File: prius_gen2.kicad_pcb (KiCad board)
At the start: 4 copper layers, 147.8 x 65 mm, 149 parts, among them J1 Conn_02x05_Odd_Even, J2 Conn_01x06, J3 Conn_01x23, J4 Conn_01x14, J5 Conn_01x03_Male, Q1 IRLZ14SPBF, Q2 IRLZ14SPBF, SW1 SW_Push, SW2 SW_Push, SW3 RESET, SW4 BOOT, U2 MCP602, U3 ULN2003A, U4 TDA2822D, U5 TJA1051T-3, U6 ESP32-WROOM-32, U7 LMR14020, U8 AZ1117-3.3, U9 STM32F103VBTx, Y1 8MHz

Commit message: started adding AD2S
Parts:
- removed C20: 1uF, Capacitor_SMD:C_0603_1608Metric
- removed C21: 100uF, Capacitor_SMD:C_Elec_6.3x7.7
- removed C22, C23, C24, C25, C27: 22n, Capacitor_SMD:C_0603_1608Metric
- removed C26: 10u, Capacitor_SMD:C_0603_1608Metric
- removed the C28 at (117.7, 113.3)
- removed the C29 at (117.7, 100.1)
- removed the C30 at (208.2, 124.3)
- removed the C31 at (180.4, 115.9)
- removed the C32 at (182.4, 115.9)
- removed the C33 at (157.3, 102.1)
- removed C45, C46, C47, C48, C49, C51, C52: 1u, Capacitor_SMD:C_0603_1608Metric
- removed the D3 at (177.2, 95.5)
- removed J5: Conn_01x03_Male, Connector_PinSocket_1.27mm:PinSocket_1x03_P1.27mm_Vertical_SMD_Pin1Left
- removed Q1, Q2: IRLZ14SPBF, Package_TO_SOT_SMD:TO-252-2
- removed the R27 at (94.6, 103.8)
- removed the R28 at (98.2, 103.8)
- removed the R29 at (101.8, 103.8)
- removed the R30 at (106.2, 107.4)
- removed the R31 at (117.7, 110.0)
- removed the R32 at (117.7, 103.4)
- removed the R34 at (208.2, 120.1)
- removed the R35 at (174.2, 95.5)
- removed the R36 at (157.4, 100.1)
- removed the R45 at (99.2, 99.5)
- removed R46, R47, R48, R49: 3.3k, Resistor_SMD:R_0603_1608Metric
- removed R50, R51, R52, R53, R54: 1.2k, Resistor_SMD:R_0603_1608Metric
- removed R56, R57, R60, R61, R62, R63: 10k, Resistor_SMD:R_0603_1608Metric
- removed SW3: RESET, Button_Switch_SMD:SW_SPST_EVQQ2
- removed SW4: BOOT, Button_Switch_SMD:SW_SPST_EVQQ2
- removed the U4 at (112.6, 106.0)
- removed the U6 at (169.0, 108.4)
- removed U9: STM32F103VBTx, Package_QFP:LQFP-100_14x14mm_P0.5mm
- added C18: 20pF, Capacitor_SMD:C_0603_1608Metric, F.Cu at (108.0, 88.2)
- added C19: 20pF, Capacitor_SMD:C_0603_1608Metric, F.Cu at (104.8, 88.2)
- added TP1: TestPoint, TestPoint:TestPoint_Keystone_5000-5004_Miniature, F.Cu at (144.5, 75.7)
- added TP2: TestPoint, TestPoint:TestPoint_Keystone_5000-5004_Miniature, F.Cu at (154.4, 86.6)
- added TP3: TestPoint, TestPoint:TestPoint_Keystone_5000-5004_Miniature, F.Cu at (166.9, 111.2)
- added TP4: TestPoint, TestPoint:TestPoint_Keystone_5000-5004_Miniature, F.Cu at (172.0, 111.2)
- added TP5: TestPoint, TestPoint:TestPoint_Keystone_5000-5004_Miniature, F.Cu at (161.9, 111.2)
- added TP6: TestPoint, TestPoint:TestPoint_Keystone_5000-5004_Miniature, F.Cu at (166.9, 106.2)
- added TP7: TestPoint, TestPoint:TestPoint_Keystone_5000-5004_Miniature, F.Cu at (161.9, 106.2)
- added U1: STM32F407VETx, Package_QFP:LQFP-100_14x14mm_P0.5mm, F.Cu at (138.2, 93.2)
- added U3: AD2S1205YSTZ, ad2s:QFP80P1200X1200X160-44N, F.Cu at (111.4, 101.2)
- added Y2: 8.192MHz, Crystal:Crystal_SMD_5032-2Pin_5.0x3.2mm, F.Cu at (106.4, 91.2)
- renumbered C7 to C10, C8 to C11, C9 to C12, C43 to C13, C44 to C14, C50 to C15, C18 to C16, C19 to C17, C13 to C28, C34 to C29, C10 to C3, C35 to C30, C36 to C31, C37 to C32, C38 to C33, C39 to C34, C40 to C35, C41 to C36, C42 to C37, C14 to C38, C15 to C39, C16 to C40, C17 to C41, C11 to C5, C12 to C6, C3 to C7, C5 to C8, C6 to C9, D7 to D1, D1 to D2, D2 to D3, JP2 to JP1, JP3 to JP2, JP1 to JP3, R44 to R10, R55 to R11, R58 to R12, R59 to R13, R22 to R14, R23 to R15, R24 to R16, R25 to R17, R26 to R18, R3 to R2, R33 to R25, R37 to R26, R38 to R27, R39 to R28, R40 to R29, R5 to R3, R6 to R30, R7 to R31, R8 to R32, R9 to R33, R10 to R34, R11 to R35, R12 to R36, R13 to R37, R14 to R38, R15 to R39, R16 to R40, R17 to R41, R18 to R42, R19 to R43, R20 to R44, R21 to R45, R64 to R5, R2 to R6, R41 to R7, R42 to R8, R43 to R9, U3 to U2, U5 to U4, U7 to U5, U8 to U6, U2 to U7
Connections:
- net Net-(J4-Pad10) renamed /Connectors/MVU
- net Net-(J4-Pad11) renamed /Connectors/MUU
- net Net-(J4-Pad9) renamed /Connectors/MWU
- J1 pad 6: Net-(J1-Pad6) -> unconnected-(J1-Pad6)
- J1 pad 7: Net-(J1-Pad7) -> unconnected-(J1-Pad7)
- J1 pad 8: Net-(J1-Pad8) -> unconnected-(J1-Pad8)
- J2 pad 6: Net-(J2-Pad6) -> unconnected-(J2-Pad6)
- J3 pad 10: /SIG_BRAKE -> unconnected-(J3-Pad10)
- J3 pad 11: /SIG_FWD -> unconnected-(J3-Pad11)
- J3 pad 12: /SIG_REV -> unconnected-(J3-Pad12)
- J3 pad 15: /OUT_DCSW -> unconnected-(J3-Pad15)
- J3 pad 16: /OUT_PRE -> unconnected-(J3-Pad16)
- J3 pad 7: /THROTTLE1 -> unconnected-(J3-Pad7)
- J3 pad 8: /THROTTLE2 -> unconnected-(J3-Pad8)
- J3 pad 9: /SIG_START -> unconnected-(J3-Pad9)
- J4 pad 8: Net-(J4-Pad8) -> unconnected-(J4-Pad8)
- U2 pad 13: Net-(J4-Pad8) -> unconnected-(U2-Pad13)
- U2 pad 14: Net-(U3-Pad14) -> unconnected-(U2-Pad14)
- U2 pad 3: Net-(U3-Pad3) -> unconnected-(U2-Pad3)
- U2 pad 4: /TIM1_CH2N -> unconnected-(U2-Pad4)
- U2 pad 9: Net-(U3-Pad9) -> unconnected-(U2-Pad9)
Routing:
- net /ADC9: track 84.0 -> 0.00 mm, vias 2 -> 0
- net /ADC11: track 81.5 -> 0.00 mm, vias 2 -> 0
- net /ADC10: track 78.4 -> 0.00 mm, vias 2 -> 0
- net /PC13: track 68.9 -> 0.00 mm, vias 2 -> 0
- net Net-(J4-Pad8): track 65.3 -> 0.00 mm
- net +3V3: track 280.0 -> 214.7 mm, vias 18 -> 15
- net unconnected-(J4-Pad8): track 0.00 -> 62.1 mm
- net Net-(C33-Pad1) (its old number): track 54.9 -> 0.00 mm, vias 2 -> 0
- net /ADC2: track 52.0 -> 0.00 mm, vias 2 -> 0
- net /ADC3: track 48.7 -> 0.00 mm, vias 2 -> 0
- net /ADC4: track 48.2 -> 0.00 mm, vias 2 -> 0
- net GND: track 121.7 -> 75.4 mm, vias 124 -> 75
- net /REV: track 44.9 -> 0.00 mm, vias 2 -> 0
- net /TIM4_CH1: track 43.8 -> 0.00 mm, vias 2 -> 0
- net /TIM3_ETR: track 42.1 -> 0.00 mm
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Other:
- board text added: "Prius G2 rev 4 2022-12"
- board text added: "github.com/ksmola/PriusG2"
- board text removed: "DCSW"
- board text removed: "ESP"
- board text removed: "FIL"
- board text removed: "PRE"
- board text removed: "Prius G2 rev 3 2021-08"
- board text removed: "TH2"
- board text removed: "powered by openinverter.org github.com/ksmola/PriusG2"

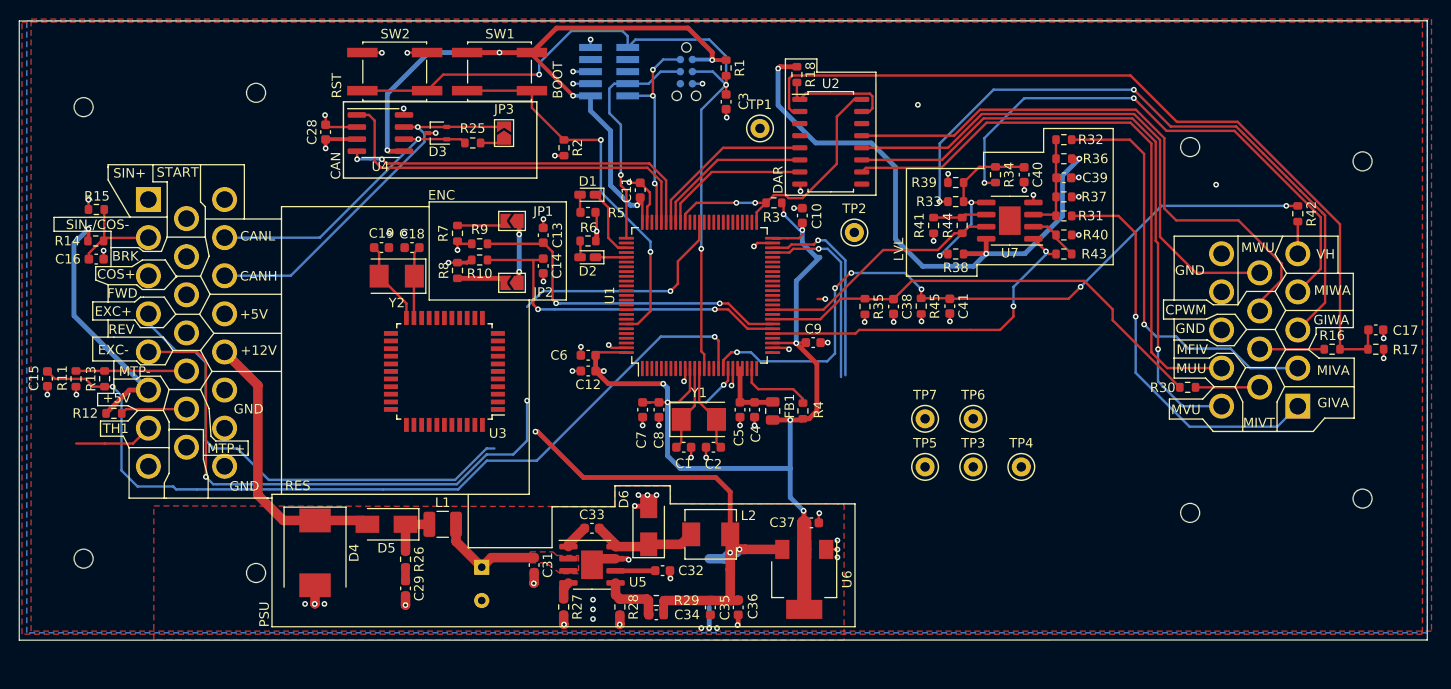
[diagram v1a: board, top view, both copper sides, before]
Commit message: routed ad2s
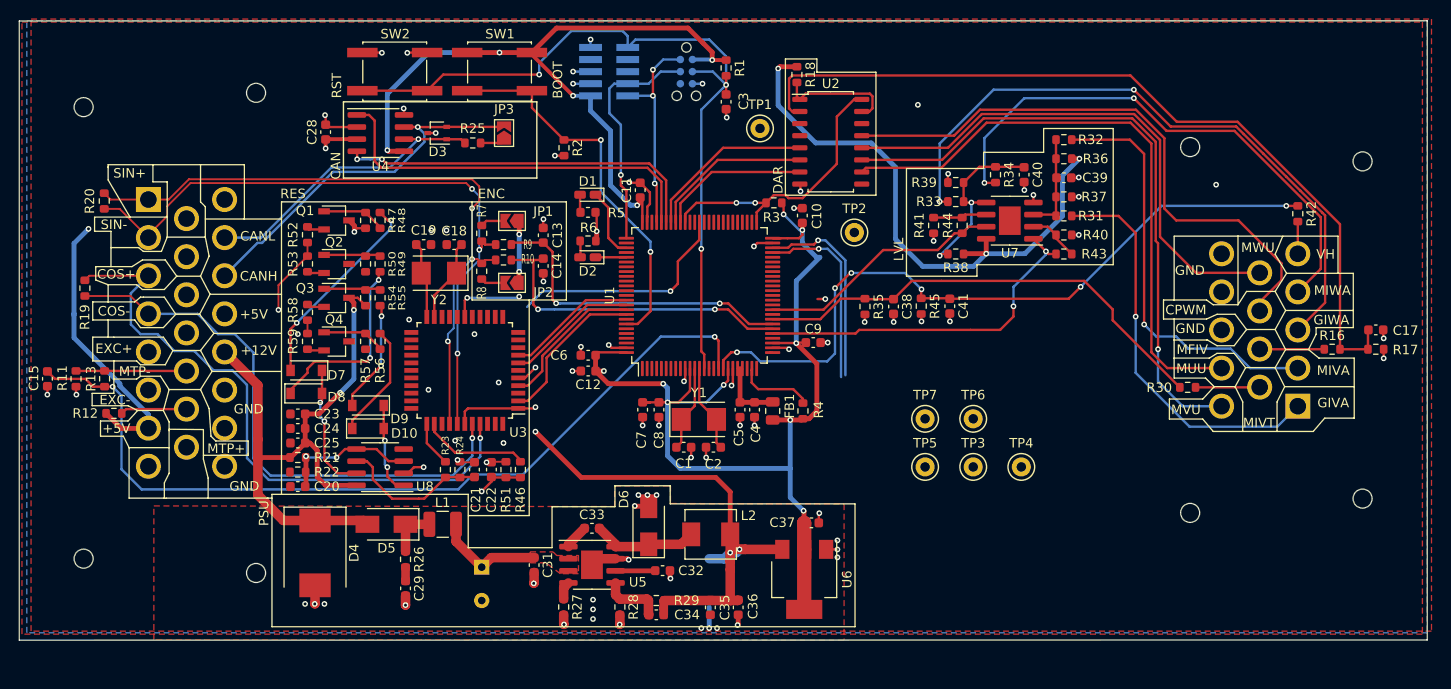
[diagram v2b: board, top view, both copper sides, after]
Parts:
- removed C16: 10uF, Capacitor_SMD:C_0603_1608Metric
- removed R14: 510, Resistor_SMD:R_0603_1608Metric
- removed R15: 220, Resistor_SMD:R_0603_1608Metric
- added C20: .1uF, Capacitor_SMD:C_0603_1608Metric, F.Cu at (96.0, 113.3)
- added C21: 120pF, Capacitor_SMD:C_0603_1608Metric, F.Cu at (114.6, 111.5)
- added C22: 120pF, Capacitor_SMD:C_0603_1608Metric, F.Cu at (116.3, 111.5)
- added C23: 1uF 12mR, Capacitor_SMD:C_0603_1608Metric, F.Cu at (96.0, 105.7)
- added C24: 1uF 12mR, Capacitor_SMD:C_0603_1608Metric, F.Cu at (96.0, 107.2)
- added C25: 10nF, Capacitor_SMD:C_0603_1608Metric, F.Cu at (96.0, 108.7)
- added D10: D, Diode_SMD:D_SOD-123, F.Cu at (103.4, 107.2)
- added D7: D, Diode_SMD:D_SOD-123, F.Cu at (96.9, 101.1)
- added D8: D, Diode_SMD:D_SOD-123, F.Cu at (96.9, 103.5)
- added D9: D, Diode_SMD:D_SOD-123, F.Cu at (103.4, 104.8)
- added Q1: Q_NPN_BEC, Package_TO_SOT_SMD:TSOT-23, F.Cu at (100.1, 85.3)
- added Q2: Q_PNP_BEC, Package_TO_SOT_SMD:TSOT-23, F.Cu at (100.1, 89.9)
- added Q3: Q_NPN_BEC, Package_TO_SOT_SMD:TSOT-23, F.Cu at (100.1, 93.5)
- added Q4: Q_PNP_BEC, Package_TO_SOT_SMD:TSOT-23, F.Cu at (100.1, 98.0)
- added R19: 68k, Resistor_SMD:R_0603_1608Metric, F.Cu at (73.7, 92.5)
- added R20: 68k, Resistor_SMD:R_0603_1608Metric, F.Cu at (75.7, 83.3)
- added R21: 22k, Resistor_SMD:R_0603_1608Metric, F.Cu at (96.0, 110.2)
- added R22: 10k, Resistor_SMD:R_0603_1608Metric, F.Cu at (96.0, 111.8)
- added R23: 10k, Resistor_SMD:R_0603_1608Metric, F.Cu at (111.5, 111.5)
- added R24: R, Resistor_SMD:R_0603_1608Metric, F.Cu at (113.0, 111.5)
- added R46: 10k, Resistor_SMD:R_0603_1608Metric, F.Cu at (119.4, 111.5)
- added R47: 2k2, Resistor_SMD:R_0603_1608Metric, F.Cu at (103.1, 85.3)
- added R48: 3r3, Resistor_SMD:R_0603_1608Metric, F.Cu at (104.6, 85.3)
- added R49: 3r3, Resistor_SMD:R_0603_1608Metric, F.Cu at (104.6, 89.9)
- added R50: 2k2, Resistor_SMD:R_0603_1608Metric, F.Cu at (103.1, 89.9)
- added R51: R, Resistor_SMD:R_0603_1608Metric, F.Cu at (117.9, 111.5)
- added R52: 4r7, Resistor_SMD:R_0603_1608Metric, F.Cu at (97.0, 86.8)
- added R53: 4r7, Resistor_SMD:R_0603_1608Metric, F.Cu at (97.0, 89.9)
- added R54: 2k2, Resistor_SMD:R_0603_1608Metric, F.Cu at (103.1, 93.5)
- added R55: 3r3, Resistor_SMD:R_0603_1608Metric, F.Cu at (104.6, 93.5)
- added R56: 3r3, Resistor_SMD:R_0603_1608Metric, F.Cu at (104.6, 98.0)
- added R57: 2k2, Resistor_SMD:R_0603_1608Metric, F.Cu at (103.1, 98.0)
- added R58: 4r7, Resistor_SMD:R_0603_1608Metric, F.Cu at (97.0, 95.0)
- added R59: 4r7, Resistor_SMD:R_0603_1608Metric, F.Cu at (97.0, 98.0)
- added U8: AD8676xR, Package_SO:SOIC-8_3.9x4.9mm_P1.27mm, F.Cu at (104.6, 111.3)
- C18, C19: value 20pF -> 22pF
- moved C18 4.43 mm to (112.4, 87.9)
- moved C19 4.43 mm to (109.2, 87.9)
- moved Y2 4.43 mm to (110.8, 90.9)
- moved R8 2.54 mm to (115.3, 90.7)
- moved R7 2.54 mm to (115.3, 86.7)
- moved R9 2.50 mm to (117.6, 87.9)
- moved R10 2.50 mm to (117.6, 89.5)
- moved U3 2.14 mm to (113.5, 101.1)
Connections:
- C13 pad 1: /TIM3_CH2 -> /Input Filter/TIM3_CH2
- C14 pad 1: /TIM3_CH1 -> /Input Filter/TIM3_CH1
- C38 pad 1: /ADC14 -> /Level Shifting/ADC14
- C41 pad 1: /ADC13 -> /Level Shifting/ADC13
- J3 pad 1: /ENC_B -> /SIN+
- J3 pad 2: Net-(C16-Pad1) -> /SIN-
- J3 pad 3: /ENC_A -> /COS+
- J3 pad 4: /R1 -> /COS-
- J3 pad 5: /R2 -> /EXC+
- J3 pad 6: +5V -> /EXC-
- J3 pad 7: unconnected-(J3-Pad7) -> +5V
- R10 pad 1: /TIM3_CH1 -> /Input Filter/TIM3_CH1
- R10 pad 2: /ENC_A -> /SIN+
- R11 pad 1: /MTEMP- -> /Input Filter/MTEMP-
- R12 pad 1: /MTEMP+ -> /Input Filter/MTEMP+
- R13 pad 1: /MTEMP- -> /Input Filter/MTEMP-
- R30 pad 1: /ADC14 -> /Level Shifting/ADC14
- R30 pad 2: /MIVT -> /Level Shifting/MIVT
- R31 pad 2: /Connectors/GIVA -> /Level Shifting/GIVA
- R32 pad 2: /Connectors/MIVA -> /Level Shifting/MIVA
- R33 pad 2: /Connectors/GIWA -> /Level Shifting/GIWA
- R34 pad 2: /Connectors/MIWA -> /Level Shifting/MIWA
- R35 pad 1: /ADC14 -> /Level Shifting/ADC14
- R42 pad 1: /ADC13 -> /Level Shifting/ADC13
- R42 pad 2: /VH -> /Level Shifting/VH
- R43 pad 2: /ADC5 -> /Level Shifting/ADC5
- R44 pad 2: /ADC8 -> /Level Shifting/ADC8
- R45 pad 1: /ADC13 -> /Level Shifting/ADC13
- R7 pad 2: /ENC_B -> /SIN-
- R8 pad 2: /ENC_A -> /SIN+
- R9 pad 1: /TIM3_CH2 -> /Input Filter/TIM3_CH2
- R9 pad 2: /ENC_B -> /SIN-
- U1 pad 89: unconnected-(U1-Pad89) -> /SCLK
- U1 pad 90: unconnected-(U1-Pad90) -> /MISO
- U1 pad 91: unconnected-(U1-Pad91) -> /~{SAMPLE}
- U1 pad 92: unconnected-(U1-Pad92) -> /~{CS}
- U3 pad 34: unconnected-(U3-Pad34) -> /Resolver/T_EXC
- U3 pad 35: unconnected-(U3-Pad35) -> /Resolver/~{T_EXC}
- U3 pad 36: unconnected-(U3-Pad36) -> GND
- U3 pad 37: /Resolver/SIN -> /SIN+
- U3 pad 38: /Resolver/~{SIN} -> /SIN-
- U3 pad 39: unconnected-(U3-Pad39) -> +5V
- U3 pad 40: /Resolver/~{COS} -> /COS-
- U3 pad 41: /Resolver/COS -> /COS+
- U3 pad 42: unconnected-(U3-Pad42) -> GND
- U4 pad 1: /CAN_TX -> /Communication/TXDCAN
- U4 pad 4: /CAN_RX -> /Communication/RXDCAN
- U7 pad 1: /ADC5 -> /Level Shifting/ADC5
- U7 pad 7: /ADC8 -> /Level Shifting/ADC8
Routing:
- net /Level Shifting/ADC13: track 0.00 -> 75.5 mm, vias 0 -> 6
- net /ADC13: track 75.5 -> 0.00 mm, vias 6 -> 0
- net /SIN-: track 0.00 -> 72.4 mm, vias 0 -> 3
- net /SIN+: track 0.00 -> 70.4 mm, vias 0 -> 3
- net /Level Shifting/GIWA: track 0.00 -> 68.4 mm, vias 0 -> 2
- net /Connectors/GIWA: track 68.4 -> 0.00 mm, vias 2 -> 0
- net /COS+: track 0.00 -> 65.1 mm, vias 0 -> 1
- net /COS-: track 0.00 -> 60.2 mm, vias 0 -> 1
- net /R2: track 58.7 -> 0.00 mm, vias 2 -> 0
- net /EXC+: track 0.00 -> 51.2 mm, vias 0 -> 2
- net /R1: track 50.3 -> 0.00 mm
- net /Level Shifting/ADC14: track 0.00 -> 49.8 mm
- net /ADC14: track 49.8 -> 0.00 mm
- net /EXC-: track 0.00 -> 49.3 mm, vias 0 -> 2
- net +12V: track 29.7 -> 76.6 mm, vias 0 -> 3
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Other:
- board text added: "COS-"
- board text added: "SIN-"
- board text removed: "BRK"
- board text removed: "FWD"
- board text removed: "REV"
- board text removed: "SIN-/COS-"
- board text removed: "START"
- board text removed: "TH1"

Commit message: cleaned up board
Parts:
- TP1, TP2, TP3, TP4, TP5, TP6, TP7: moved to B.Cu
- moved R32 45.1 mm to (183.4, 121.4), turned to -90 degrees
- moved R36 42.8 mm to (181.4, 121.4), turned to 90 degrees
- moved C39 40.7 mm to (179.4, 121.4), turned to -90 degrees
- moved R37 38.6 mm to (177.4, 121.4), turned to -90 degrees
- moved C40 37.5 mm to (179.7, 117.2), turned to 180 degrees
- moved R31 36.6 mm to (175.4, 121.4), turned to -90 degrees
- moved R34 35.3 mm to (179.7, 114.2), turned to 180 degrees
- moved R40 34.7 mm to (173.4, 121.4), turned to -90 degrees
- moved R43 32.9 mm to (171.4, 121.4), turned to 90 degrees
- moved R39 31.9 mm to (178.9, 110.1), turned to 90 degrees
- moved U7 30.7 mm to (174.9, 115.7), turned to 90 degrees
- moved TP3 30.4 mm to (153.7, 83.9), turned to 180 degrees
- moved R33 29.2 mm to (176.9, 110.1), turned to 90 degrees
- moved R44 26.3 mm to (174.4, 110.7), turned to 180 degrees
- moved R41 24.8 mm to (174.4, 107.7), turned to 180 degrees
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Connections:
- C13 pad 1: /Input Filter/TIM3_CH2 -> /TIM3_CH2
- C14 pad 1: /Input Filter/TIM3_CH1 -> /TIM3_CH1
- C38 pad 1: /Level Shifting/ADC14 -> /ADC14
- C41 pad 1: /Level Shifting/ADC13 -> /ADC13
- R10 pad 1: /Input Filter/TIM3_CH1 -> /TIM3_CH1
- R11 pad 1: /Input Filter/MTEMP- -> /MTEMP-
- R12 pad 1: /Input Filter/MTEMP+ -> /MTEMP+
- R13 pad 1: /Input Filter/MTEMP- -> /MTEMP-
- R30 pad 1: /Level Shifting/ADC14 -> /ADC14
- R30 pad 2: /Level Shifting/MIVT -> /MIVT
- R31 pad 2: /Level Shifting/GIVA -> /Connectors/GIVA
- R32 pad 2: /Level Shifting/MIVA -> /Connectors/MIVA
- R33 pad 2: /Level Shifting/GIWA -> /Connectors/GIWA
- R34 pad 2: /Level Shifting/MIWA -> /Connectors/MIWA
- R35 pad 1: /Level Shifting/ADC14 -> /ADC14
- R42 pad 1: /Level Shifting/ADC13 -> /ADC13
- R42 pad 2: /Level Shifting/VH -> /VH
- R43 pad 2: /Level Shifting/ADC5 -> /ADC5
- R44 pad 2: /Level Shifting/ADC8 -> /ADC8
- R45 pad 1: /Level Shifting/ADC13 -> /ADC13
- R9 pad 1: /Input Filter/TIM3_CH2 -> /TIM3_CH2
- U3 pad 2: /Resolver/~{RD} -> /~{CS}
- U3 pad 4: /Resolver/~{SAMPLE} -> /~{SAMPLE}
- U3 pad 7: /Resolver/SO -> /MISO
- U3 pad 8: /Resolver/SCLK -> /SCLK
- U4 pad 1: /Communication/TXDCAN -> /CAN_TX
- U4 pad 4: /Communication/RXDCAN -> /CAN_RX
- U7 pad 1: /Level Shifting/ADC5 -> /ADC5
- U7 pad 7: /Level Shifting/ADC8 -> /ADC8
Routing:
- net /Level Shifting/ADC13: track 75.5 -> 0.00 mm, vias 6 -> 0
- net /Level Shifting/GIWA: track 68.4 -> 0.00 mm, vias 2 -> 0
- net +5V: track 309.4 -> 245.3 mm, vias 14 -> 11
- net unconnected-(J4-Pad8): track 62.1 -> 0.00 mm
- net /ADC13: track 0.00 -> 56.9 mm, vias 0 -> 3
- net /Level Shifting/ADC14: track 49.8 -> 0.00 mm
- net /Level Shifting/MIVA: track 44.1 -> 0.00 mm, vias 1 -> 0
- net /Level Shifting/GIVA: track 42.4 -> 0.00 mm, vias 1 -> 0
- net /Connectors/GIWA: track 0.00 -> 39.0 mm, vias 0 -> 1
- net /Communication/RXDCAN: track 38.6 -> 0.00 mm, vias 2 -> 0
- net /CAN_RX: track 0.00 -> 38.6 mm, vias 0 -> 2
- net /Level Shifting/ADC5: track 37.3 -> 0.00 mm, vias 2 -> 0
- net /TIM3_CH1: track 0.00 -> 34.3 mm, vias 0 -> 2
- net /Input Filter/TIM3_CH1: track 34.3 -> 0.00 mm, vias 2 -> 0
- net /Input Filter/TIM3_CH2: track 34.2 -> 0.00 mm, vias 2 -> 0
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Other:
- board size 147.8 x 65 mm -> 130.6 x 65 mm
- board text removed: "CPWM"
- board text removed: "LVL"

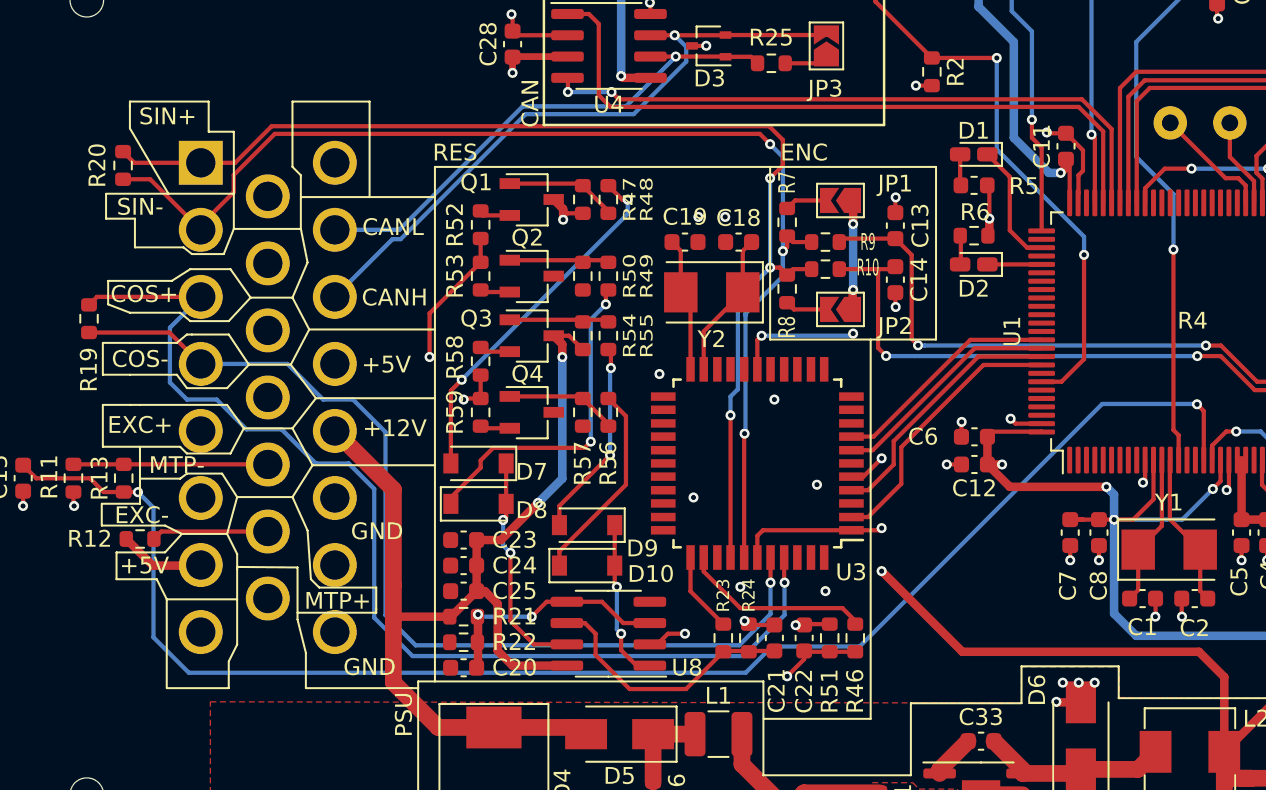
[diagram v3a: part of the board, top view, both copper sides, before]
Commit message: fixed resolver buffer circuit
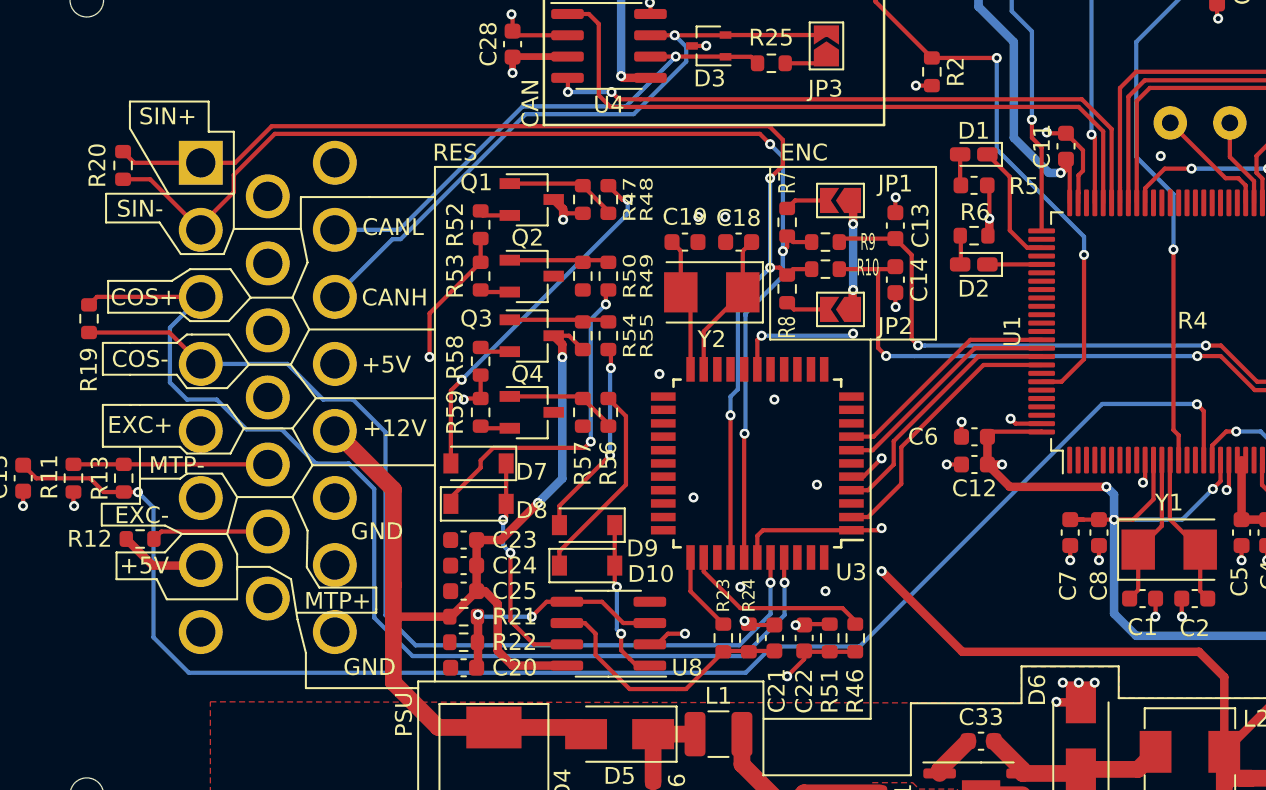
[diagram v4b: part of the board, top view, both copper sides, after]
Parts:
- renumbered TP7 to BKIN, TP6 to CH1, TP1 to CH1N, TP5 to CH2, TP2 to CH2N, TP4 to CH3, TP3 to CH3N
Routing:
- net GND: vias 74 -> 75
